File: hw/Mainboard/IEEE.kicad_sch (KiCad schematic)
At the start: 24 parts, among them J3 IEEE, U2 SN74LS07, U3 SN74LS07, U4 SN74LS07, U5 74LS245, U6 74LS245

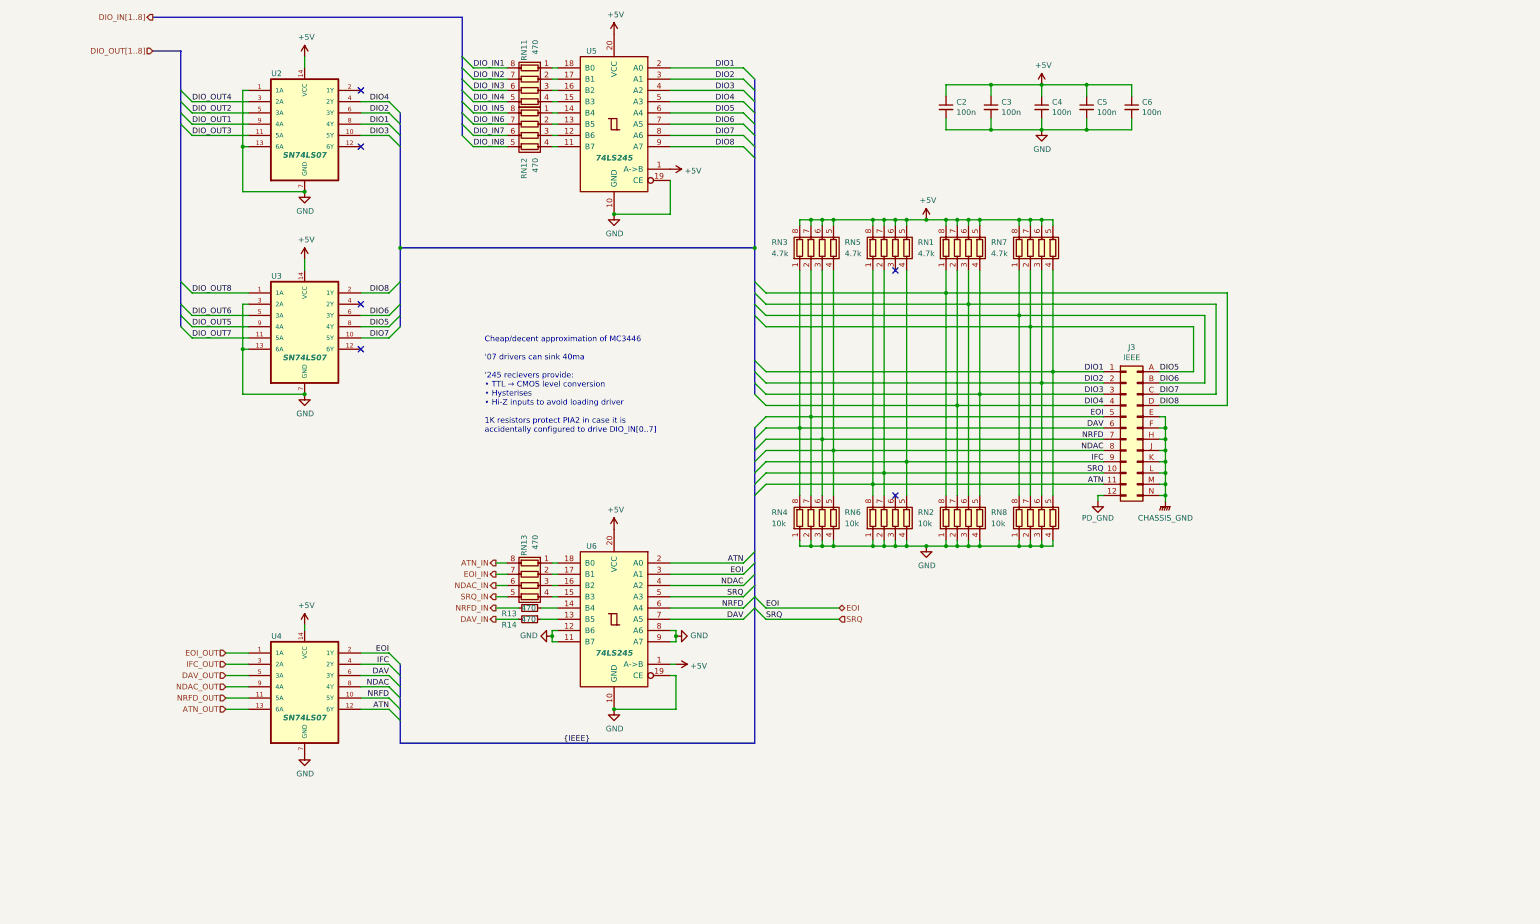
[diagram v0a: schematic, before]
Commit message: hw: larger schematic pages, routed w/netties
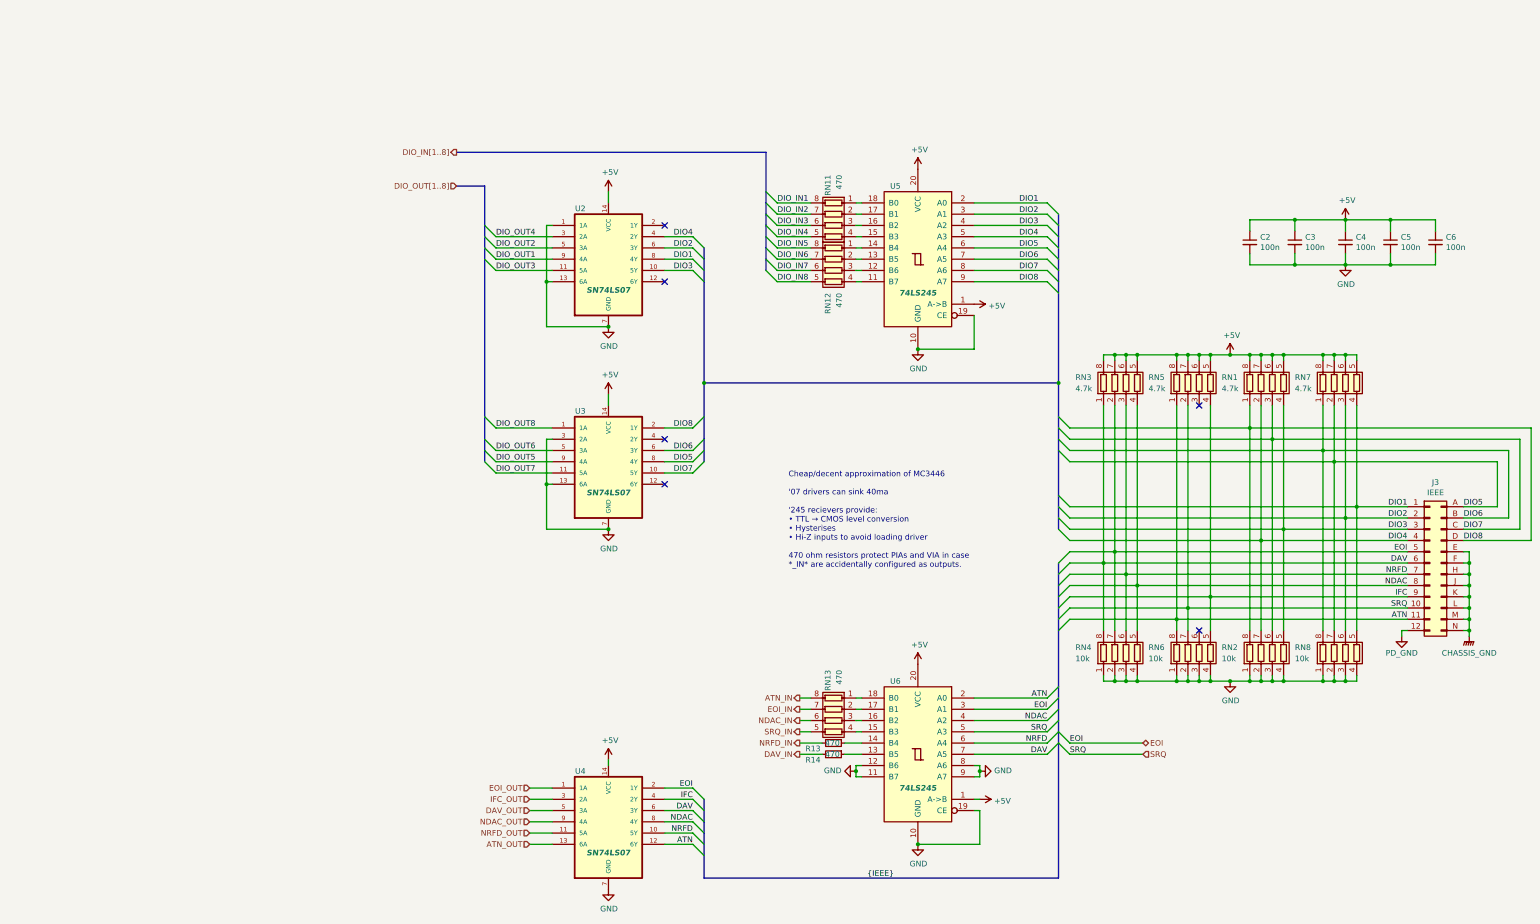
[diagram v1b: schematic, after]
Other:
- note added: "Cheap/decent approximation of MC3446 '07 drivers can sink 40ma '245 recievers provide: • TTL → CMOS level conversion • Hysterises • Hi-Z inputs to avoid loading driver 470 ohm resistors protect PIAs and VIA in case *_IN* are accidentally configured as outputs."
- note removed: "Cheap/decent approximation of MC3446 '07 drivers can sink 40ma '245 recievers provide: • TTL → CMOS level conversion • Hysterises • Hi-Z inputs to avoid loading driver 1K resistors protect PIA2 in case it is accidentally configured to drive DIO_IN[0..7]"
- moved on the sheet: C2, C3, C4, C5, C6, J3, R13, R14, RN1, RN11, RN12, RN13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

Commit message: hw: wip
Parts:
- added PT5: PowerTie_2, PET:NetTie-2_SMD_Pad_1.6_to_0.4mm, symbol PET:PowerTie_2
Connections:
- net +5V renamed VCC
- net VCC: now also PT5.2
- new net PD_5V: PT5.1

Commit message: hw: wip
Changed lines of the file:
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@@
   (paper "B")
   (bus_alias "IEEE_IN" (members "DAV_IN" "NRFD_IN" "NDAC_IN" "ATN_IN" "EOI_IN" "SRQ_IN"))
-  (bus_alias "IEEE" (members "ATN" "EOI" "NDAC" "SRQ" "NRFD" "DAV" "IFC"))
+  (bus_alias "IEEE" (members "ATN" "EOI" "NDAC" "SRQ" "NRFD" "DAV" "IFC" "DIO8" "DIO1" "DIO2" "DIO3" "DIO4" "DIO5" "DIO6" "DIO7"))
   (junction (at 328.93 153.67) (diameter 0) (color 0 0 0 0)
   )
@@
     (effects (font (size 1.27 1.27)) (justify left bottom))
   )
+  (label "{IEEE}" (at 194.31 100.33 0)
+    (effects (font (size 1.27 1.27)) (justify left bottom))
+  )

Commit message: jlcpcb - 1/19
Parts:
- U2, U3, U4: MOUSER 595-SN74LS07DR -> (none)
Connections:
- net VCC is gone; now on net PD_5V: C2.1, C3.1, C4.1, C5.1, C6.1, PT5.2, RN1.5 (R4.2), RN1.6 (R3.2), RN1.7 (R2.2), RN1.8 (R1.2), RN3.5 (R4.2), RN3.6 (R3.2), RN3.7 (R2.2), RN3.8 (R1.2), RN5.5 (R4.2), RN5.6 (R3.2), RN5.7 (R2.2), RN5.8 (R1.2), RN7.5 (R4.2), RN7.6 (R3.2), RN7.7 (R2.2), RN7.8 (R1.2), U2.14 (VCC), U3.14 (VCC), U4.14 (VCC), U5.1 (A->B), U5.20 (VCC), U6.1 (A->B), U6.20 (VCC)
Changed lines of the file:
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@@
+    (stroke (width 0) (type default) (color 0 0 0 0))
+  )
+  (wire (pts (xy 321.31 62.23) (xy 321.31 63.5))
     (stroke (width 0) (type default) (color 0 0 0 0))
   )
@@
       (effects (font (size 1.27 1.27)) hide)
     )
-    (property "Datasheet" "https://datasheet.lcsc.com/lcsc/1810010228_Texas-Instruments-SN74LS245DWR_C129580.pdf" (id 3) (at 204.47 72.39 0)
+    (property "Datasheet" "~" (id 3) (at 204.47 72.39 0)
       (effects (font (size 1.27 1.27)) hide)
     )
@@
       (effects (font (size 1.27 1.27)) hide)
     )
-    (property "Datasheet" "https://datasheet.lcsc.com/lcsc/1810010228_Texas-Instruments-SN74LS245DWR_C129580.pdf" (id 3) (at 204.47 184.15 0)
+    (property "Datasheet" "~" (id 3) (at 204.47 184.15 0)
       (effects (font (size 1.27 1.27)) hide)
     )
@@
       (effects (font (size 1.27 1.27)) hide)
     )
-    (property "MOUSER" "595-SN74LS07DR" (id 5) (at 139.7 204.47 0)
+    (property "MOUSER" "" (id 5) (at 139.7 204.47 0)
       (effects (font (size 1.27 1.27)) hide)
     )
@@
       (effects (font (size 1.27 1.27)) hide)
     )
-    (property "Datasheet" "~" (id 3) (at 279.4 68.58 0)
+    (property "Datasheet" "https://datasheet.lcsc.com/lcsc/1810191219_Samsung-Electro-Mechanics-CL05B104KO5NNNC_C1525.pdf" (id 3) (at 279.4 68.58 0)
       (effects (font (size 1.27 1.27)) hide)
     )
@@
       (effects (font (size 1.27 1.27)) hide)
     )
-    (property "Datasheet" "~" (id 3) (at 289.56 68.58 0)
+    (property "Datasheet" "https://datasheet.lcsc.com/lcsc/1810191219_Samsung-Electro-Mechanics-CL05B104KO5NNNC_C1525.pdf" (id 3) (at 289.56 68.58 0)
       (effects (font (size 1.27 1.27)) hide)
     )
@@
       (effects (font (size 1.27 1.27)) hide)
     )
-    (property "Datasheet" "~" (id 3) (at 300.99 68.58 0)
+    (property "Datasheet" "https://datasheet.lcsc.com/lcsc/1810191219_Samsung-Electro-Mechanics-CL05B104KO5NNNC_C1525.pdf" (id 3) (at 300.99 68.58 0)
       (effects (font (size 1.27 1.27)) hide)
     )
@@
       (effects (font (size 1.27 1.27)) hide)
     )
-    (property "Datasheet" "~" (id 3) (at 311.15 68.58 0)
+    (property "Datasheet" "https://datasheet.lcsc.com/lcsc/1810191219_Samsung-Electro-Mechanics-CL05B104KO5NNNC_C1525.pdf" (id 3) (at 311.15 68.58 0)
       (effects (font (size 1.27 1.27)) hide)
     )
@@
       (effects (font (size 1.27 1.27)) hide)
     )
-    (property "Datasheet" "~" (id 3) (at 321.31 68.58 0)
+    (property "Datasheet" "https://datasheet.lcsc.com/lcsc/1810191219_Samsung-Electro-Mechanics-CL05B104KO5NNNC_C1525.pdf" (id 3) (at 321.31 68.58 0)
       (effects (font (size 1.27 1.27)) hide)
     )
@@
       (effects (font (size 1.27 1.27)) hide)
     )
-    (property "MOUSER" "595-SN74LS07DR" (id 5) (at 139.7 123.19 0)
+    (property "MOUSER" "" (id 5) (at 139.7 123.19 0)
       (effects (font (size 1.27 1.27)) hide)
     )
@@
       (effects (font (size 1.27 1.27)) hide)
     )
-    (property "MOUSER" "595-SN74LS07DR" (id 5) (at 139.7 77.47 0)
+    (property "MOUSER" "" (id 5) (at 139.7 77.47 0)
       (effects (font (size 1.27 1.27)) hide)
     )
@@
       (effects (font (size 1.27 1.27)) hide)
     )
-    (property "Datasheet" "~" (id 3) (at 185.42 181.61 0)
+    (property "Datasheet" "https://datasheet.lcsc.com/lcsc/2205311900_UNI-ROYAL-Uniroyal-Elec-0402WGF4700TCE_C25117.pdf" (id 3) (at 185.42 181.61 0)
       (effects (font (size 1.27 1.27)) hide)
     )
@@
       (effects (font (size 1.27 1.27)) hide)
     )
-    (property "Datasheet" "" (id 3) (at 185.42 74.93 0)
+    (property "Datasheet" "https://datasheet.lcsc.com/lcsc/1809301140_UNI-ROYAL-Uniroyal-Elec-4D03WGJ0471T5E_C25510.pdf" (id 3) (at 185.42 74.93 0)
       (effects (font (size 1.27 1.27)) hide)
     )
@@
       (effects (font (size 1.27 1.27)) hide)
     )
-    (property "Datasheet" "" (id 3) (at 185.42 64.77 0)
+    (property "Datasheet" "https://datasheet.lcsc.com/lcsc/1809301140_UNI-ROYAL-Uniroyal-Elec-4D03WGJ0471T5E_C25510.pdf" (id 3) (at 185.42 64.77 0)
       (effects (font (size 1.27 1.27)) hide)
     )
@@
       (effects (font (size 1.27 1.27)) hide)
     )
-    (property "Datasheet" "" (id 3) (at 185.42 176.53 0)
+    (property "Datasheet" "https://datasheet.lcsc.com/lcsc/1809301140_UNI-ROYAL-Uniroyal-Elec-4D03WGJ0471T5E_C25510.pdf" (id 3) (at 185.42 176.53 0)
       (effects (font (size 1.27 1.27)) hide)
     )
@@
       (effects (font (size 1.27 1.27)) hide)
     )
-    (property "Datasheet" "~" (id 3) (at 185.42 184.15 0)
+    (property "Datasheet" "https://datasheet.lcsc.com/lcsc/2205311900_UNI-ROYAL-Uniroyal-Elec-0402WGF4700TCE_C25117.pdf" (id 3) (at 185.42 184.15 0)
       (effects (font (size 1.27 1.27)) hide)
     )
@@
       (effects (font (size 1.27 1.27)) hide)
     )
+    (pin "1")
+  )
+  (symbol (lib_id "PET:PD_5V") (at 321.31 62.23 0) (unit 1)
+    (in_bom yes) (on_board yes) (fields_autoplaced)
+    (property "Reference" "#PWR0239" (id 0) (at 321.31 66.04 0)
+      (effects (font (size 1.27 1.27)) hide)
+    )
+    (property "Value" "PD_5V" (id 1) (at 321.31 57.15 0))
+    (property "Footprint" "" (id 2) (at 321.31 62.23 0)
+      (effects (font (size 1.27 1.27)) hide)
+    )
+    (property "Datasheet" "" (id 3) (at 321.31 62.23 0)
+      (effects (font (size 1.27 1.27)) hide)
+    )

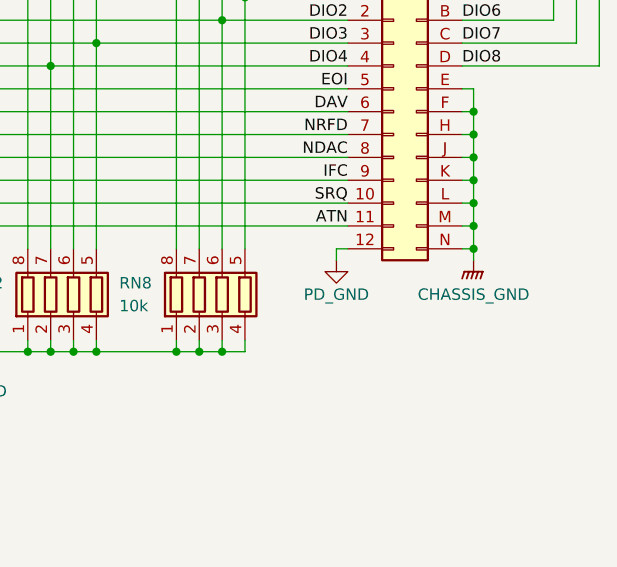
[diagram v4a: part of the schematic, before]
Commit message: hw: fix reversed signal and chassis gnd on IEEE
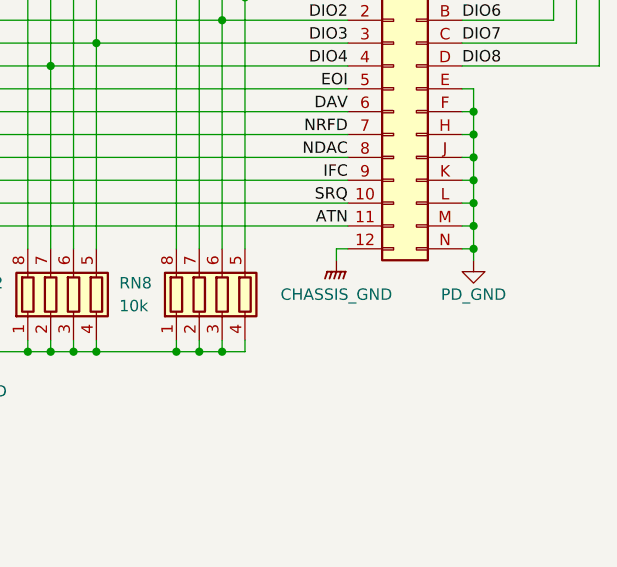
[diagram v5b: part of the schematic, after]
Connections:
- net CHASSIS_GND: now also J3.12 (GND); no longer J3.E (GND), J3.F (GND), J3.H (GND), J3.J (GND), J3.K (GND), J3.L (GND), J3.M (GND), J3.N (GND)
- net PD_GND: now also J3.E (GND), J3.F (GND), J3.H (GND), J3.J (GND), J3.K (GND), J3.L (GND), J3.M (GND), J3.N (GND); no longer J3.12 (GND)
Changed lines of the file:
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@@
     (pin "2")
   )
-  (symbol (lib_id "PET:PD_GND") (at 313.69 157.48 0) (unit 1)
-    (in_bom yes) (on_board yes)
-    (property "Reference" "#PWR0183" (id 0) (at 313.69 163.83 0)
-      (effects (font (size 1.27 1.27)) hide)
-    )
-    (property "Value" "PD_GND" (id 1) (at 313.69 161.29 0))
-    (property "Footprint" "" (id 2) (at 313.69 157.48 0)
-      (effects (font (size 1.27 1.27)) hide)
-    )
-    (property "Datasheet" "" (id 3) (at 313.69 157.48 0)
+  (symbol (lib_id "PET:PD_GND") (at 328.93 157.48 0) (unit 1)
+    (in_bom yes) (on_board yes)
+    (property "Reference" "#PWR0183" (id 0) (at 328.93 163.83 0)
+      (effects (font (size 1.27 1.27)) hide)
+    )
+    (property "Value" "PD_GND" (id 1) (at 328.93 161.29 0))
+    (property "Footprint" "" (id 2) (at 328.93 157.48 0)
+      (effects (font (size 1.27 1.27)) hide)
+    )
+    (property "Datasheet" "" (id 3) (at 328.93 157.48 0)
       (effects (font (size 1.27 1.27)) hide)
     )
@@
     (pin "1")
   )
-  (symbol (lib_id "PET:CHASSIS_GND") (at 328.93 157.48 0) (unit 1)
-    (in_bom yes) (on_board yes)
-    (property "Reference" "#PWR0184" (id 0) (at 328.93 162.56 0)
-      (effects (font (size 1.27 1.27)) hide)
-    )
-    (property "Value" "CHASSIS_GND" (id 1) (at 328.93 161.29 0))
-    (property "Footprint" "" (id 2) (at 328.93 158.75 0)
-      (effects (font (size 1.27 1.27)) hide)
-    )
-    (property "Datasheet" "" (id 3) (at 328.93 158.75 0)
-      (effects (font (size 1.27 1.27)) hide)
-    )
+  (symbol (lib_id "PET:CHASSIS_GND") (at 313.69 157.48 0) (unit 1)
+    (in_bom yes) (on_board yes)
+    (property "Reference" "#PWR0184" (id 0) (at 313.69 162.56 0)
+      (effects (font (size 1.27 1.27)) hide)
+    )
+    (property "Value" "CHASSIS_GND" (id 1) (at 313.69 161.29 0))
+    (property "Footprint" "" (id 2) (at 313.69 158.75 0)
+      (effects (font (size 1.27 1.27)) hide)
+    )
+    (property "Datasheet" "" (id 3) (at 313.69 158.75 0)
+      (effects (font (size 1.27 1.27)) hide)
+    )

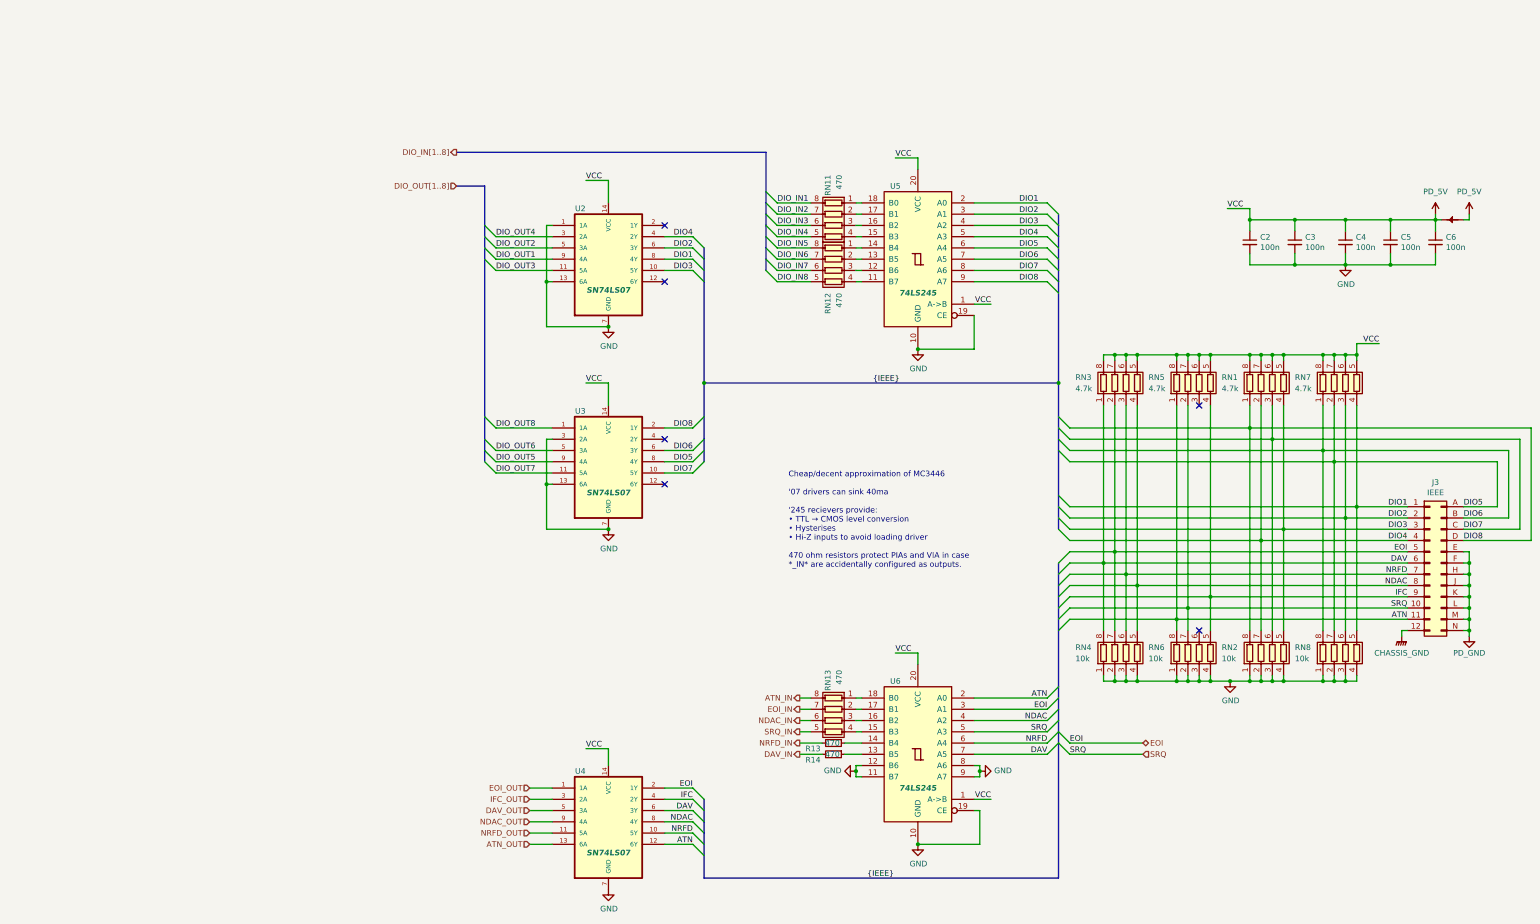
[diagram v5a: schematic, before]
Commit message: hw: tidy power and resize pages
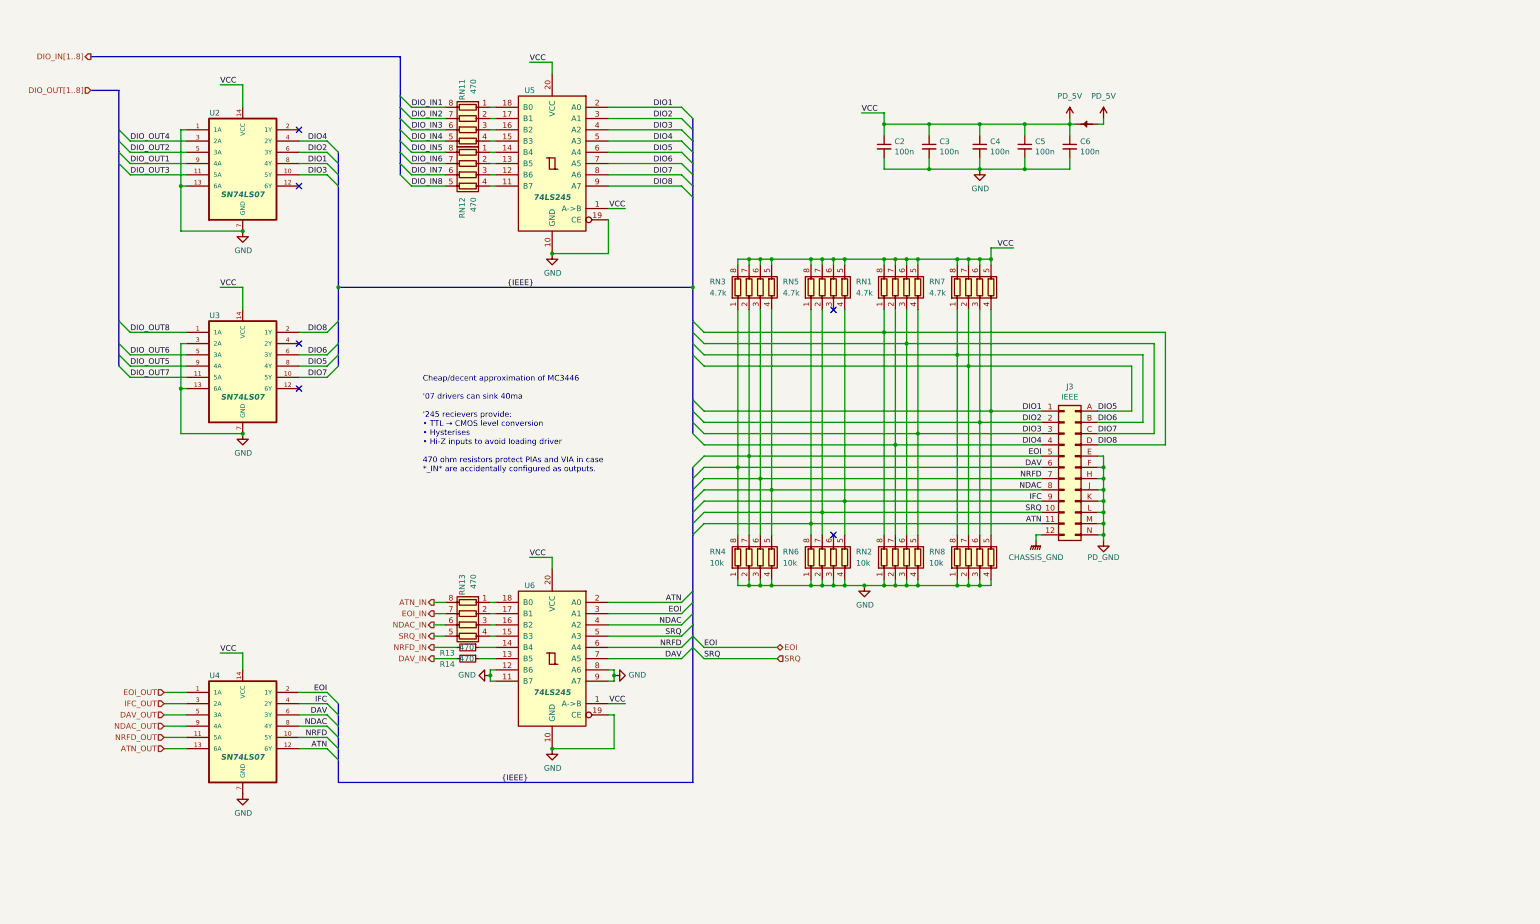
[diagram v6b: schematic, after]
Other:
- title: (none) -> CBM PET Mainboard Replacement
- moved on the sheet: C2, C3, C4, C5, C6, J3, R13, R14, RN1, RN11, RN12, RN13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
